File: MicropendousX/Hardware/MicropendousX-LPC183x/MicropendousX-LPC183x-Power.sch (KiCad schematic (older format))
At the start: 62 parts, among them IC1 LPC183X, IC2 STC3100, IC6 LTC3559, Q1 Si2312, Q2 FDN304

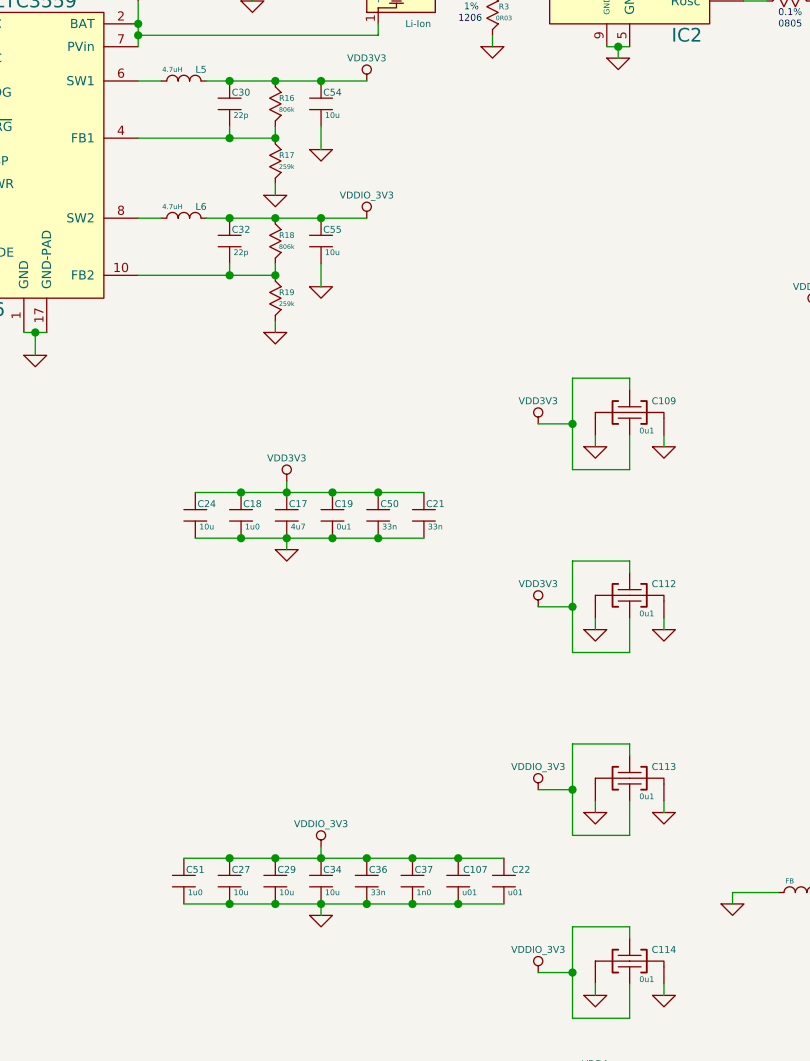
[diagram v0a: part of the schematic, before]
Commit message: Updated MicropendousX-LPC183x portable design with minor post-prototyping corrections.
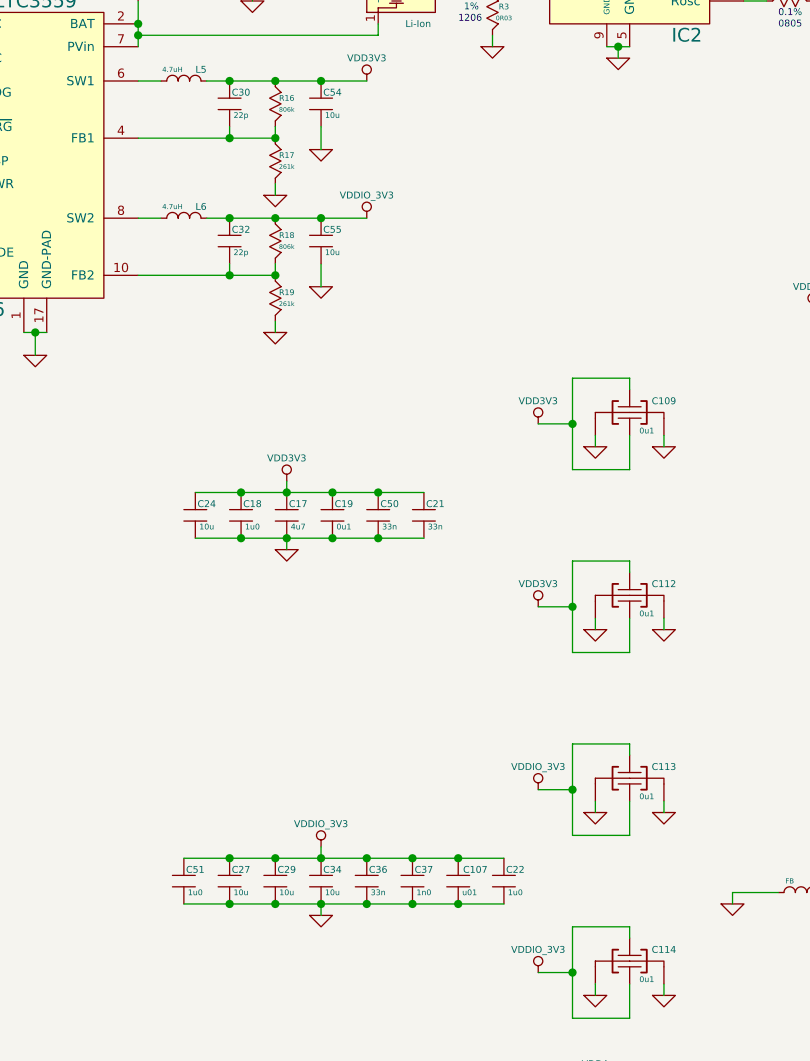
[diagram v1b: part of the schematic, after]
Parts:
- C22: value u01 -> 1u0
- R17, R19: value 259k -> 261k
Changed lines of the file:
@@
-EESchema Schematic File Version 2  date 9/26/2011 2:10:54 AM
+EESchema Schematic File Version 2  date 11/3/2011 5:56:20 AM
 LIBS:power
 LIBS:device
@@
 Sheet 6 7
 Title "MicropendousX-LPC183x"
-Date "26 sep 2011"
+Date "3 nov 2011"
 Rev "1.0"
 Comp "Opendous Inc."
@@
 U 1 1 4E7FE693
 P 5650 5750
-F 0 "C22" V 5600 5825 30  0000 C CNN
-F 1 "u01" V 5700 5800 25  0000 C CNN
+F 0 "C22" V 5600 5800 30  0000 C CNN
+F 1 "1u0" V 5700 5800 25  0000 C CNN
 	1    5650 5750
 	0    1    1    0
@@
 P 4650 3200
 F 0 "R19" V 4625 3250 25  0000 C CNN
-F 1 "259k" V 4675 3250 20  0000 C CNN
+F 1 "261k" V 4675 3250 20  0000 C CNN
 	1    4650 3200
 	0    1    1    0
@@
 P 4650 2600
 F 0 "R17" V 4625 2650 25  0000 C CNN
-F 1 "259k" V 4675 2650 20  0000 C CNN
+F 1 "261k" V 4675 2650 20  0000 C CNN
 	1    4650 2600
 	0    1    1    0
